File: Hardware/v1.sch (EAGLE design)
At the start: 78 parts, among them IC1 LM324D, IC2 m328p, IC3 REG1117, J1 22-27-2061-06, J2 22-27-2021-02, J3 22-27-2021-02, J4 22-27-2031-03, J5 22-27-2041-04, Q1 BSS123, Q2 BSS123, Q3 BSS123, Q5 BSS123

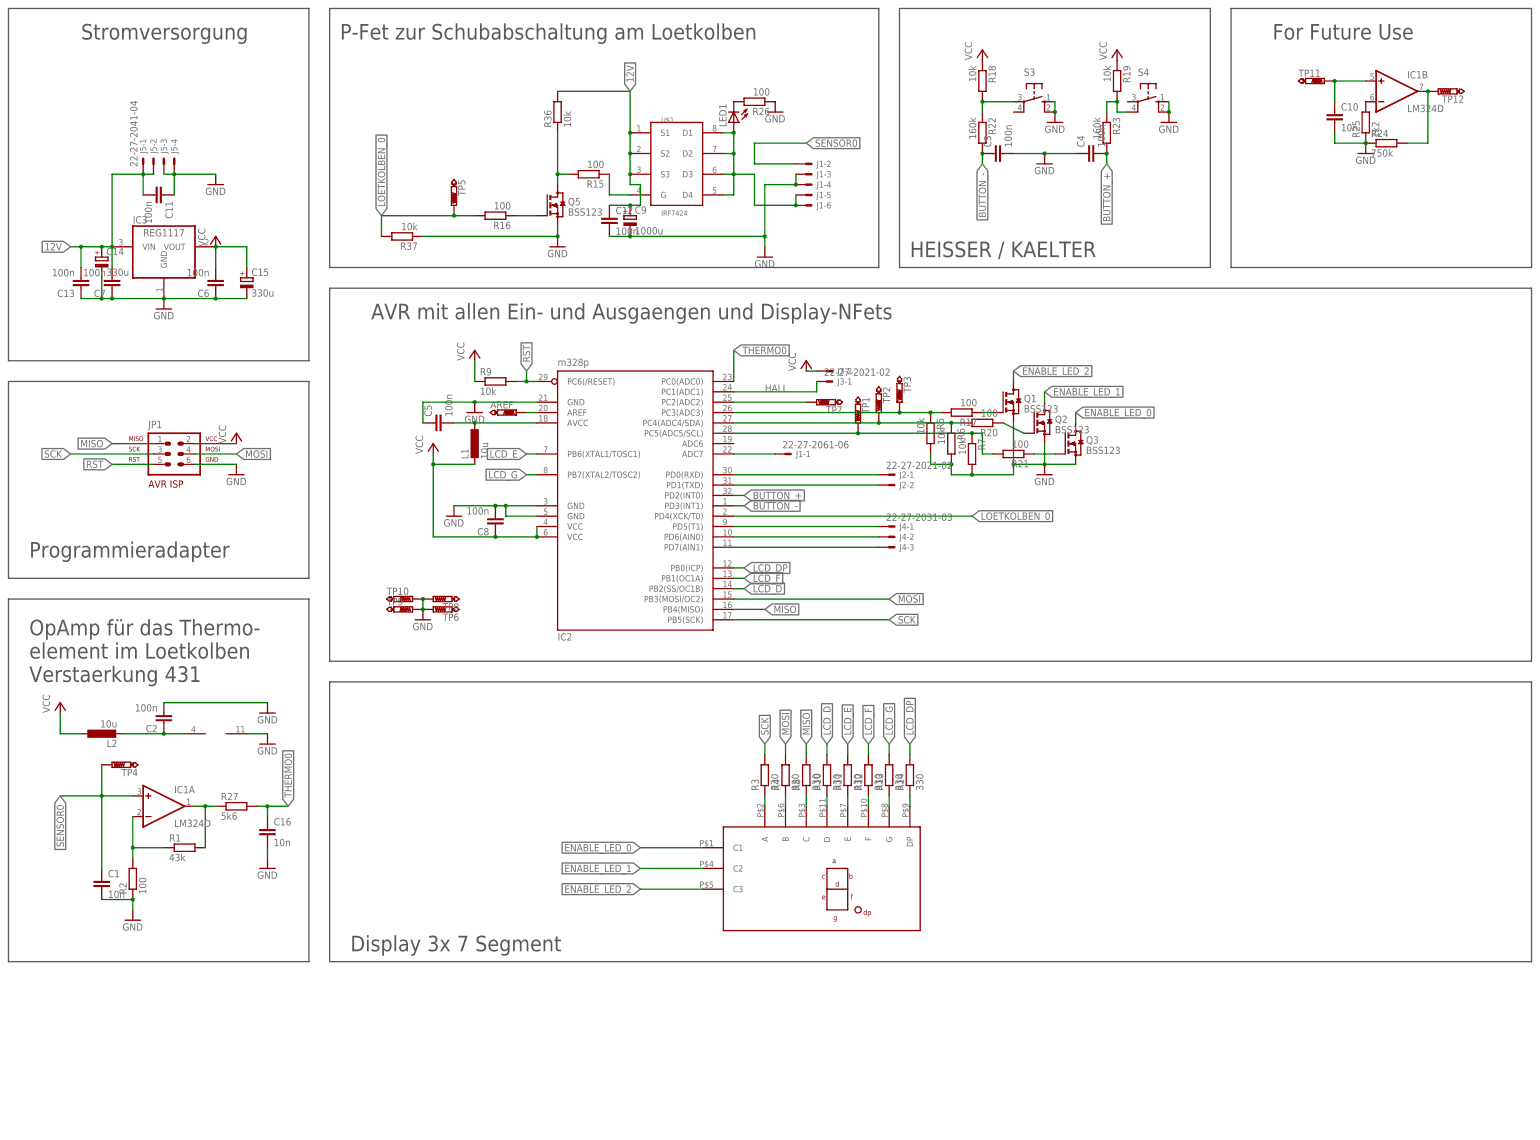
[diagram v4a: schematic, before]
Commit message: some resistor sizes changed from 0402 to 0603
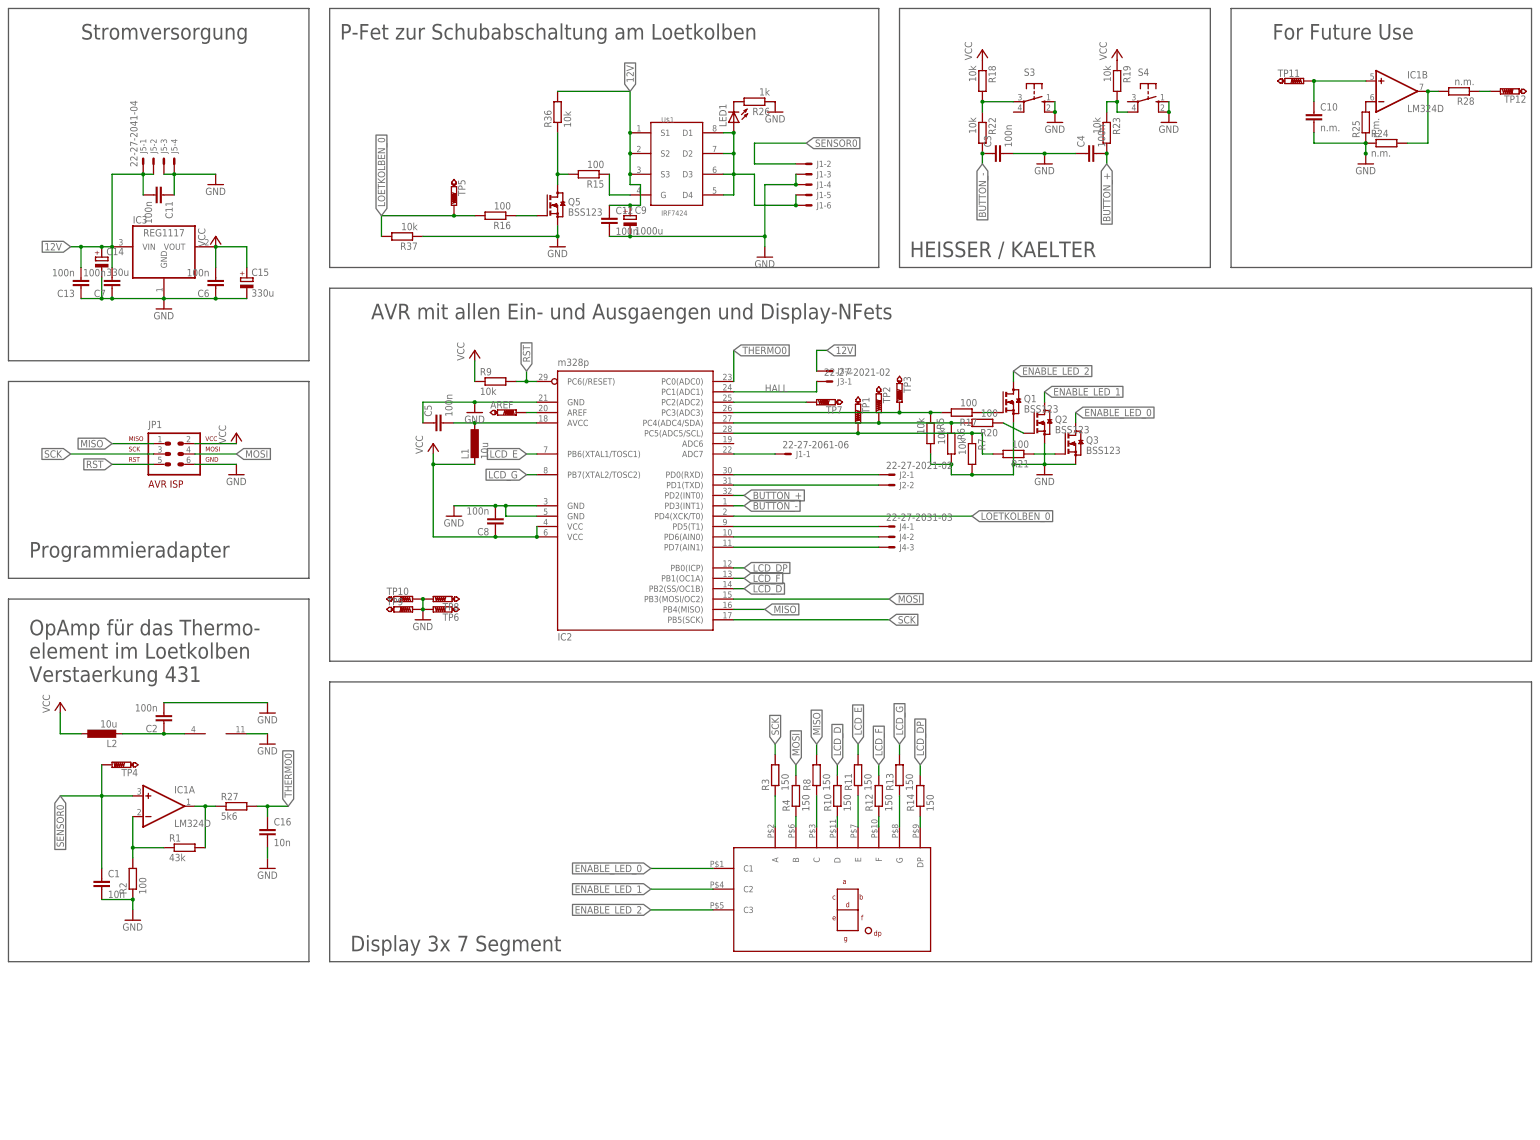
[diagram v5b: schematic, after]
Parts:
- added R28: n.m., rcl:R-EU_R0603
- C10: value 10n -> n.m.
- LED1: device eagle-ltspice:LED_ESML0603 -> led:LEDCHIP-LED0805
- R10, R11, R12, R13, R14, R3, R4, R8: value 330 -> 150
- R22, R23: value 160k -> 10k
- R24: value 750k -> n.m.
- R25: value 1k2 -> n.m.
- R26: value 100 -> 1k
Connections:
- new net N$21: R28.1, TP12.TP
- net 12V: now also J3-2.S
- net N$26: now also R28.2; no longer TP12.TP
- net VCC: no longer J3-2.S
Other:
- moved on the sheet: C10, R10, R11, R12, R13, R14, R3, R4, R8, TP11, TP12

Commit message: finalized
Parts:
- R18, R19, R36, R37, R5, R6, R7, R9: device rcl:R-EU_R0402 -> rcl:R-EU_R0603
- R27: value 5k6 -> 10k
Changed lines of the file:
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@@
 <part name="GND6" library="supply1" deviceset="GND" device=""/>
 <part name="GND7" library="supply1" deviceset="GND" device=""/>
-<part name="R9" library="rcl" deviceset="R-EU_" device="R0402" value="10k"/>
+<part name="R9" library="rcl" deviceset="R-EU_" device="R0603" value="10k"/>
 <part name="P+2" library="supply1" deviceset="VCC" device=""/>
 <part name="C5" library="rcl" deviceset="C-EU" device="C0603" value="100n"/>
@@
 <part name="C8" library="rcl" deviceset="C-EU" device="C0603" value="100n"/>
 <part name="Q5" library="transistor-small-signal" deviceset="BSS123" device=""/>
-<part name="R36" library="rcl" deviceset="R-EU_" device="R0402" value="10k"/>
-<part name="R37" library="rcl" deviceset="R-EU_" device="R0402" value="10k"/>
+<part name="R36" library="rcl" deviceset="R-EU_" device="R0603" value="10k"/>
+<part name="R37" library="rcl" deviceset="R-EU_" device="R0603" value="10k"/>
 <part name="GND13" library="supply1" deviceset="GND" device=""/>
 <part name="GND15" library="supply1" deviceset="GND" device=""/>
-<part name="R18" library="rcl" deviceset="R-EU_" device="R0402" value="10k"/>
+<part name="R18" library="rcl" deviceset="R-EU_" device="R0603" value="10k"/>
 <part name="P+6" library="supply1" deviceset="VCC" device=""/>
-<part name="R19" library="rcl" deviceset="R-EU_" device="R0402" value="10k"/>
+<part name="R19" library="rcl" deviceset="R-EU_" device="R0603" value="10k"/>
 <part name="P+7" library="supply1" deviceset="VCC" device=""/>
 <part name="GND8" library="supply1" deviceset="GND" device=""/>
@@
 <part name="Q3" library="transistor-small-signal" deviceset="BSS123" device=""/>
 <part name="GND10" library="supply1" deviceset="GND" device=""/>
-<part name="R5" library="rcl" deviceset="R-EU_" device="R0402" value="10k"/>
-<part name="R6" library="rcl" deviceset="R-EU_" device="R0402" value="10k"/>
-<part name="R7" library="rcl" deviceset="R-EU_" device="R0402" value="10k"/>
+<part name="R5" library="rcl" deviceset="R-EU_" device="R0603" value="10k"/>
+<part name="R6" library="rcl" deviceset="R-EU_" device="R0603" value="10k"/>
+<part name="R7" library="rcl" deviceset="R-EU_" device="R0603" value="10k"/>
 <part name="C15" library="rcl" deviceset="CPOL-EU" device="E2-5" value="330u"/>
 <part name="TP1" library="testpad" deviceset="PTR1" device="B1,27"/>
@@
 <part name="C16" library="rcl" deviceset="C-EU" device="C0603" value="10n"/>
 <part name="GND17" library="supply1" deviceset="GND" device=""/>
-<part name="R27" library="rcl" deviceset="R-EU_" device="R0603" value="5k6"/>
+<part name="R27" library="rcl" deviceset="R-EU_" device="R0603" value="10k"/>
 <part name="TP7" library="testpad" deviceset="PTR1" device="B1,27"/>
 <part name="R28" library="rcl" deviceset="R-EU_" device="R0603" value="n.m."/>
